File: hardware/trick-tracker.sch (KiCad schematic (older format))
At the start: 52 parts, among them J1 USB4105-GF-A, J2 S2B-PH-K, J3 QWiiC, J4 MEM2051-00-195-00-A, J5 Debug, J6 QWiiC, P1 SMTB-1240-S-R, U1 MS88SF2, U2 DPS368XTSA1, U3 LSM9DS1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

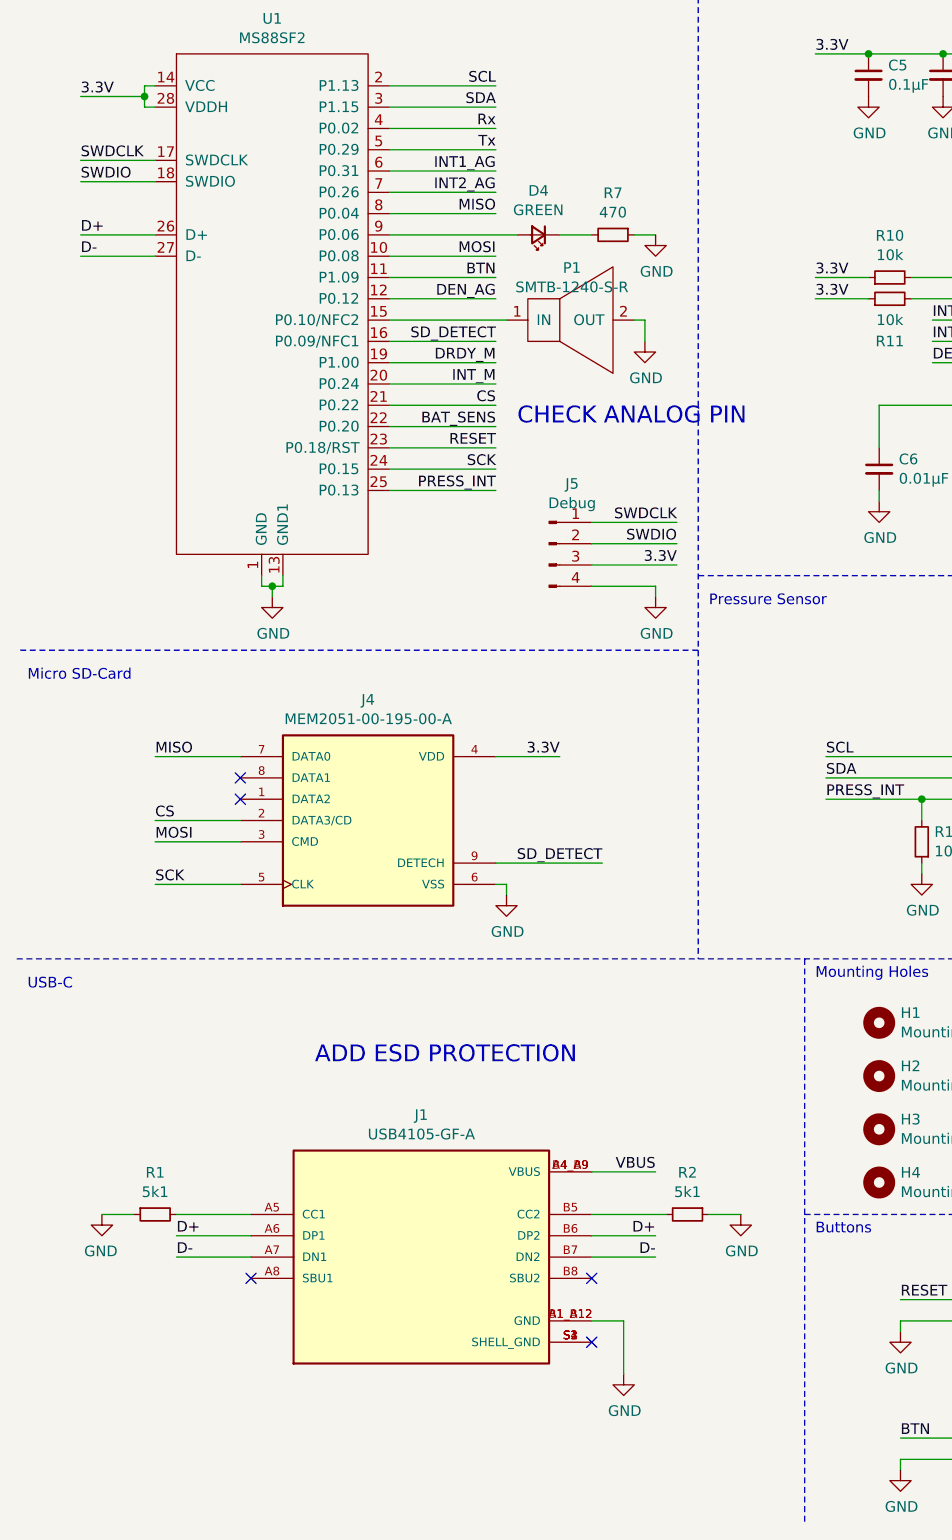
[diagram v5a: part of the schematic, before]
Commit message: Fix BAT_SENS and added it to an ADC - exchanged with an interrupt
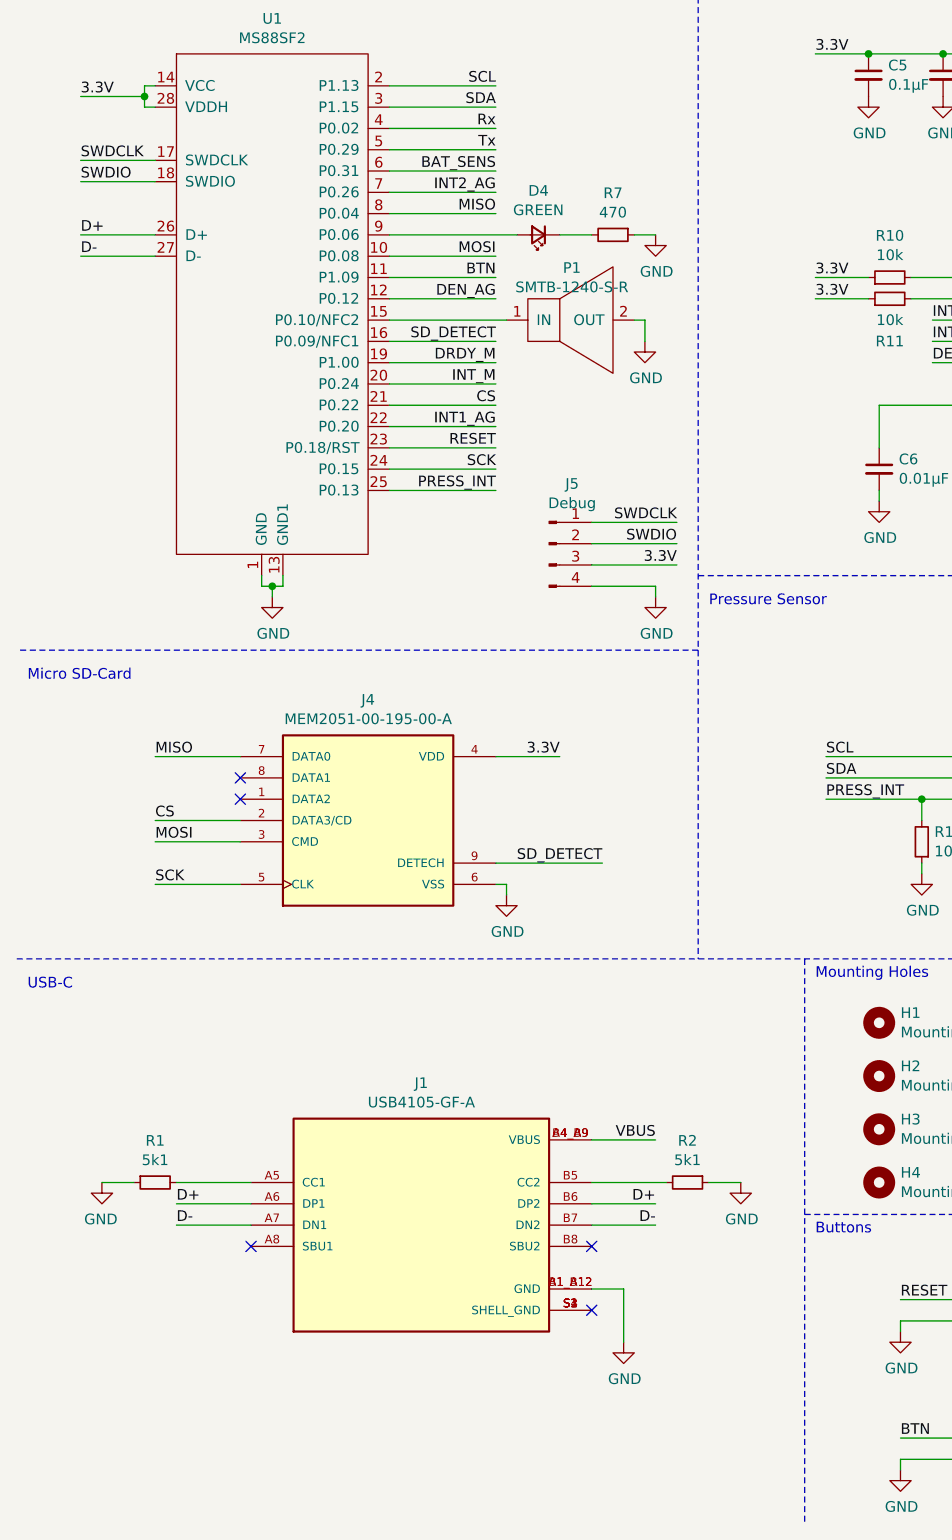
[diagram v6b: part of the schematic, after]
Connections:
- net BAT_SENS: now also U1.6 (P0.31); no longer U1.22 (P0.20)
- net INT1_AG: now also U1.22 (P0.20); no longer U1.6 (P0.31)
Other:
- note removed: "ADD ESD PROTECTION"
- note removed: "CHECK ANALOG PIN"
- moved on the sheet: J1, R1, R2
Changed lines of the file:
@@
 L USB4105-GF-A:USB4105-GF-A J1
 U 1 1 60A97D83
-P 2400 6550
-F 0 "J1" H 2400 7217 50  0000 C CNN
-F 1 "USB4105-GF-A" H 2400 7126 50  0000 C CNN
-F 2 "USB4105-GF-A:GCT_USB4105-GF-A" H 2400 6550 50  0001 L BNN
-F 3 "" H 2400 6550 50  0001 L BNN
-F 4 "A3" H 2400 6550 50  0001 L BNN "PARTREV"
-F 5 "3.31 mm" H 2400 6550 50  0001 L BNN "MAXIMUM_PACKAGE_HEIGHT"
-F 6 "Manufacturer Recommendations" H 2400 6550 50  0001 L BNN "STANDARD"
-F 7 "GCT" H 2400 6550 50  0001 L BNN "MANUFACTURER"
-	1    2400 6550
+P 2400 6400
+F 0 "J1" H 2400 7067 50  0000 C CNN
+F 1 "USB4105-GF-A" H 2400 6976 50  0000 C CNN
+F 2 "USB4105-GF-A:GCT_USB4105-GF-A" H 2400 6400 50  0001 L BNN
+F 3 "" H 2400 6400 50  0001 L BNN
+F 4 "A3" H 2400 6400 50  0001 L BNN "PARTREV"
+F 5 "3.31 mm" H 2400 6400 50  0001 L BNN "MAXIMUM_PACKAGE_HEIGHT"
+F 6 "Manufacturer Recommendations" H 2400 6400 50  0001 L BNN "STANDARD"
+F 7 "GCT" H 2400 6400 50  0001 L BNN "MANUFACTURER"
+	1    2400 6400
 	1    0    0    -1
 $EndComp
@@
 Wire Wire Line
 	10350 1700 10100 1700
-Text Label 3500 6150 2    50   ~ 0
+Text Label 3500 6000 2    50   ~ 0
 VBUS
-Text Label 3500 6450 2    50   ~ 0
+Text Label 3500 6300 2    50   ~ 0
 D+
-Text Label 3500 6550 2    50   ~ 0
+Text Label 3500 6400 2    50   ~ 0
 D-
-NoConn ~ 3200 6950
+NoConn ~ 3200 6800
 $Comp
 L power:GND #PWR0104
 U 1 1 60AA70B4
-P 3350 7100
-F 0 "#PWR0104" H 3350 6850 50  0001 C CNN
-F 1 "GND" H 3355 6927 50  0000 C CNN
-F 2 "" H 3350 7100 50  0001 C CNN
-F 3 "" H 3350 7100 50  0001 C CNN
-	1    3350 7100
-	1    0    0    -1
-$EndComp
-NoConn ~ 3200 6650
-NoConn ~ 1600 6650
-Text Label 1250 6450 0    50   ~ 0
+P 3350 6950
+F 0 "#PWR0104" H 3350 6700 50  0001 C CNN
+F 1 "GND" H 3355 6777 50  0000 C CNN
+F 2 "" H 3350 6950 50  0001 C CNN
+F 3 "" H 3350 6950 50  0001 C CNN
+	1    3350 6950
+	1    0    0    -1
+$EndComp
+NoConn ~ 3200 6500
+NoConn ~ 1600 6500
+Text Label 1250 6300 0    50   ~ 0
 D+
-Text Label 1250 6550 0    50   ~ 0
+Text Label 1250 6400 0    50   ~ 0
 D-
 Wire Wire Line
-	3500 6450 3200 6450
-Wire Wire Line
-	3500 6550 3200 6550
-Wire Wire Line
-	1600 6550 1250 6550
-Wire Wire Line
-	1250 6450 1600 6450
-Wire Wire Line
-	3500 6150 3200 6150
-Wire Wire Line
-	3200 6850 3350 6850
-Wire Wire Line
-	3350 6850 3350 7100
+	3500 6300 3200 6300
+Wire Wire Line
+	3500 6400 3200 6400
+Wire Wire Line
+	1600 6400 1250 6400
+Wire Wire Line
+	1250 6300 1600 6300
+Wire Wire Line
+	3500 6000 3200 6000
+Wire Wire Line
+	3200 6700 3350 6700
+Wire Wire Line
+	3350 6700 3350 6950
 Text Label 9750 2550 0    50   ~ 0
 VBUS
@@
 L Device:R_Small R1
 U 1 1 60AA9590
-P 1150 6350
-F 0 "R1" V 954 6350 50  0000 C CNN
-F 1 "5k1" V 1045 6350 50  0000 C CNN
-F 2 "Resistor_SMD:R_0603_1608Metric" H 1150 6350 50  0001 C CNN
-F 3 "~" H 1150 6350 50  0001 C CNN
-	1    1150 6350
+P 1150 6200
+F 0 "R1" V 954 6200 50  0000 C CNN
+F 1 "5k1" V 1045 6200 50  0000 C CNN
+F 2 "Resistor_SMD:R_0603_1608Metric" H 1150 6200 50  0001 C CNN
+F 3 "~" H 1150 6200 50  0001 C CNN
+	1    1150 6200
 	0    -1   1    0
 $EndComp
@@
 L Device:R_Small R2
 U 1 1 60AA9CB6
-P 3650 6350
-F 0 "R2" V 3454 6350 50  0000 C CNN
-F 1 "5k1" V 3545 6350 50  0000 C CNN
-F 2 "Resistor_SMD:R_0603_1608Metric" H 3650 6350 50  0001 C CNN
-F 3 "~" H 3650 6350 50  0001 C CNN
-	1    3650 6350
+P 3650 6200
+F 0 "R2" V 3454 6200 50  0000 C CNN
+F 1 "5k1" V 3545 6200 50  0000 C CNN
+F 2 "Resistor_SMD:R_0603_1608Metric" H 3650 6200 50  0001 C CNN
+F 3 "~" H 3650 6200 50  0001 C CNN
+	1    3650 6200
 	0    1    1    0
 $EndComp
 Wire Wire Line
-	1250 6350 1600 6350
-Wire Wire Line
-	3200 6350 3550 6350
+	1250 6200 1600 6200
+Wire Wire Line
+	3200 6200 3550 6200
 $Comp
 L power:GND #PWR0105
 U 1 1 60AAABDF
-P 3900 6350
-F 0 "#PWR0105" H 3900 6100 50  0001 C CNN
-F 1 "GND" H 3905 6177 50  0000 C CNN
-F 2 "" H 3900 6350 50  0001 C CNN
-F 3 "" H 3900 6350 50  0001 C CNN
-	1    3900 6350
+P 3900 6200
+F 0 "#PWR0105" H 3900 5950 50  0001 C CNN
+F 1 "GND" H 3905 6027 50  0000 C CNN
+F 2 "" H 3900 6200 50  0001 C CNN
+F 3 "" H 3900 6200 50  0001 C CNN
+	1    3900 6200
 	1    0    0    -1
 $EndComp
@@
 L power:GND #PWR0106
 U 1 1 60AAB5AF
-P 900 6350
-F 0 "#PWR0106" H 900 6100 50  0001 C CNN
-F 1 "GND" H 905 6177 50  0000 C CNN
-F 2 "" H 900 6350 50  0001 C CNN
-F 3 "" H 900 6350 50  0001 C CNN
-	1    900  6350
+P 900 6200
+F 0 "#PWR0106" H 900 5950 50  0001 C CNN
+F 1 "GND" H 905 6027 50  0000 C CNN
+F 2 "" H 900 6200 50  0001 C CNN
+F 3 "" H 900 6200 50  0001 C CNN
+	1    900  6200
 	-1   0    0    -1
 $EndComp
 Wire Wire Line
-	900  6350 1050 6350
-Wire Wire Line
-	3900 6350 3750 6350
+	900  6200 1050 6200
+Wire Wire Line
+	3900 6200 3750 6200
 Text Label 10900 2550 2    50   ~ 0
 STAT
@@
 Wire Wire Line
 	2750 1350 2250 1350
-Text Label 2750 1450 2    50   ~ 0
+Text Label 2750 2650 2    50   ~ 0
 INT1_AG
 Text Label 2750 1550 2    50   ~ 0
@@
 Wire Wire Line
 	9500 5800 10100 5800
-Text Label 2750 2650 2    50   ~ 0
+Text Label 2750 1450 2    50   ~ 0
 BAT_SENS
 Wire Wire Line
@@
 Wire Wire Line
 	3500 3400 3200 3400
-Text Notes 2850 2650 0    79   ~ 0
-CHECK ANALOG PIN
-Text Notes 1900 5650 0    79   ~ 0
-ADD ESD PROTECTION
 $Comp
 L SMTB-1240-S-R:SMTB-1240-S-R P1

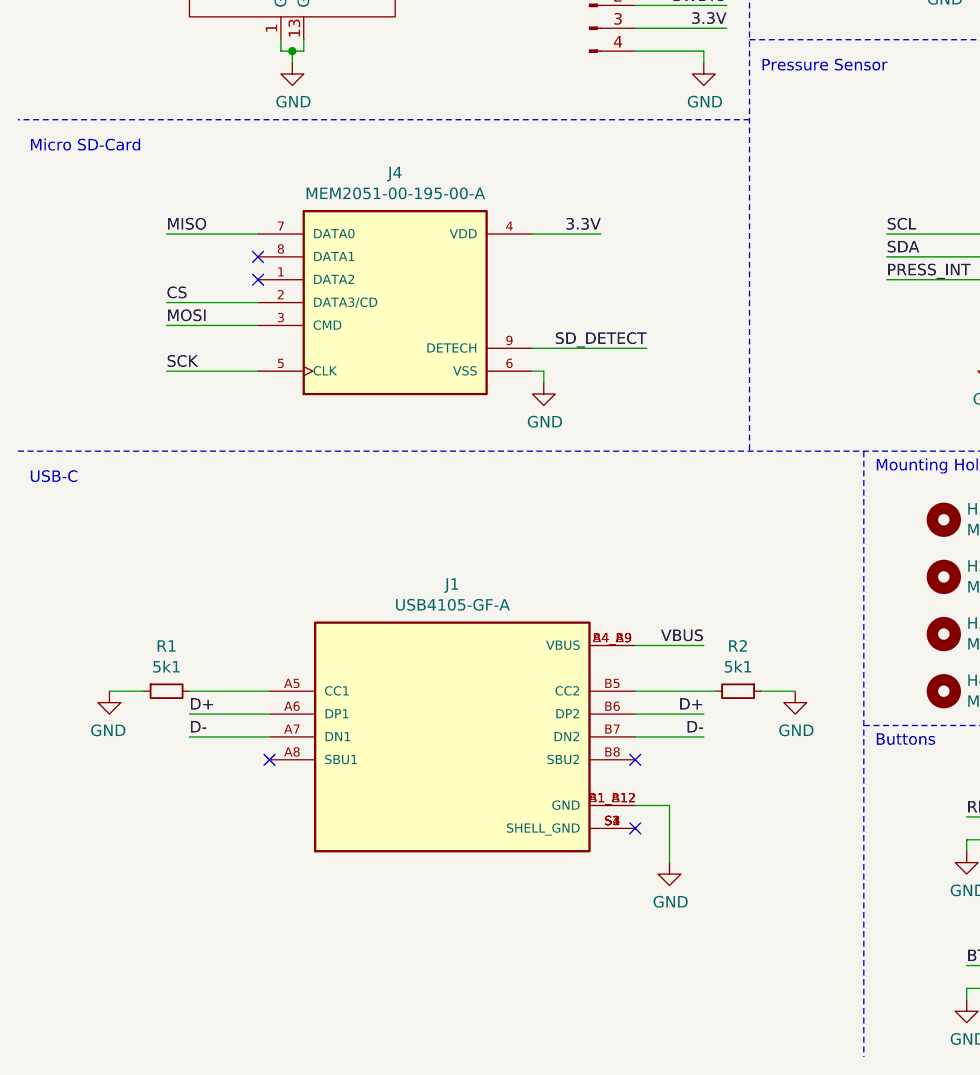
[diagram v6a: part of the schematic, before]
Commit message: Add ESD protection for USB
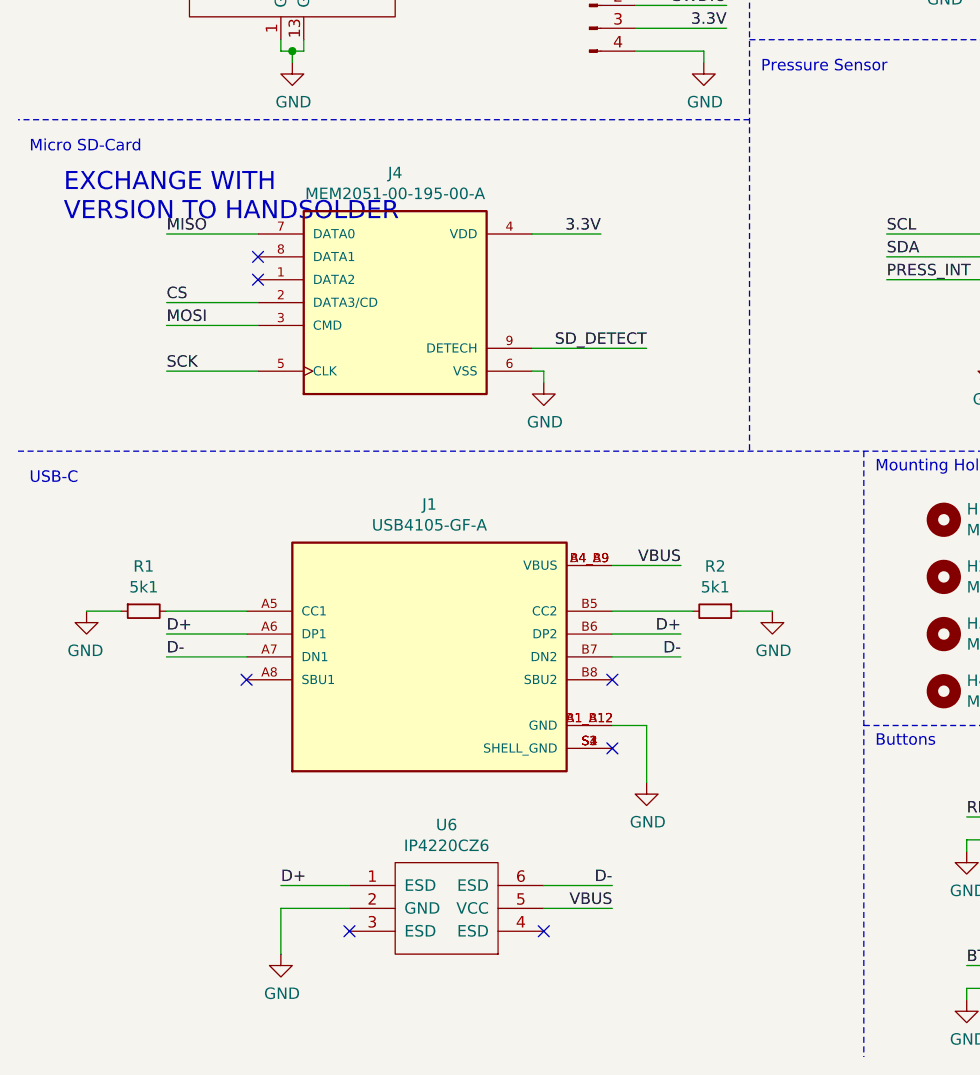
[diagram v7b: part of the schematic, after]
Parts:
- added U6: IP4220CZ6, Package_SO:TSOP-6_1.65x3.05mm_P0.95mm, symbol IP4220CZ6:IP4220CZ6
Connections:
- net D+: now also U6.1 (ESD)
- net D-: now also U6.6 (ESD)
- net GND: now also U6.2 (GND)
- net VBUS: now also U6.5 (VCC)
- no-connect marks 8 -> 10
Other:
- note added: "EXCHANGE WITH \nVERSION TO HANDSOLDER"
- moved on the sheet: J1, R1, R2
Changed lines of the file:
@@
 L USB4105-GF-A:USB4105-GF-A J1
 U 1 1 60A97D83
-P 2400 6400
-F 0 "J1" H 2400 7067 50  0000 C CNN
-F 1 "USB4105-GF-A" H 2400 6976 50  0000 C CNN
-F 2 "USB4105-GF-A:GCT_USB4105-GF-A" H 2400 6400 50  0001 L BNN
-F 3 "" H 2400 6400 50  0001 L BNN
-F 4 "A3" H 2400 6400 50  0001 L BNN "PARTREV"
-F 5 "3.31 mm" H 2400 6400 50  0001 L BNN "MAXIMUM_PACKAGE_HEIGHT"
-F 6 "Manufacturer Recommendations" H 2400 6400 50  0001 L BNN "STANDARD"
-F 7 "GCT" H 2400 6400 50  0001 L BNN "MANUFACTURER"
-	1    2400 6400
+P 2300 6050
+F 0 "J1" H 2300 6717 50  0000 C CNN
+F 1 "USB4105-GF-A" H 2300 6626 50  0000 C CNN
+F 2 "USB4105-GF-A:GCT_USB4105-GF-A" H 2300 6050 50  0001 L BNN
+F 3 "" H 2300 6050 50  0001 L BNN
+F 4 "A3" H 2300 6050 50  0001 L BNN "PARTREV"
+F 5 "3.31 mm" H 2300 6050 50  0001 L BNN "MAXIMUM_PACKAGE_HEIGHT"
+F 6 "Manufacturer Recommendations" H 2300 6050 50  0001 L BNN "STANDARD"
+F 7 "GCT" H 2300 6050 50  0001 L BNN "MANUFACTURER"
+	1    2300 6050
 	1    0    0    -1
 $EndComp
@@
 Wire Wire Line
 	10350 1700 10100 1700
-Text Label 3500 6000 2    50   ~ 0
+Text Label 3400 5650 2    50   ~ 0
 VBUS
-Text Label 3500 6300 2    50   ~ 0
+Text Label 3400 5950 2    50   ~ 0
 D+
-Text Label 3500 6400 2    50   ~ 0
+Text Label 3400 6050 2    50   ~ 0
 D-
-NoConn ~ 3200 6800
+NoConn ~ 3100 6450
 $Comp
 L power:GND #PWR0104
 U 1 1 60AA70B4
-P 3350 6950
-F 0 "#PWR0104" H 3350 6700 50  0001 C CNN
-F 1 "GND" H 3355 6777 50  0000 C CNN
-F 2 "" H 3350 6950 50  0001 C CNN
-F 3 "" H 3350 6950 50  0001 C CNN
-	1    3350 6950
-	1    0    0    -1
-$EndComp
-NoConn ~ 3200 6500
-NoConn ~ 1600 6500
-Text Label 1250 6300 0    50   ~ 0
+P 3250 6600
+F 0 "#PWR0104" H 3250 6350 50  0001 C CNN
+F 1 "GND" H 3255 6427 50  0000 C CNN
+F 2 "" H 3250 6600 50  0001 C CNN
+F 3 "" H 3250 6600 50  0001 C CNN
+	1    3250 6600
+	1    0    0    -1
+$EndComp
+NoConn ~ 3100 6150
+NoConn ~ 1500 6150
+Text Label 1150 5950 0    50   ~ 0
 D+
-Text Label 1250 6400 0    50   ~ 0
+Text Label 1150 6050 0    50   ~ 0
 D-
 Wire Wire Line
-	3500 6300 3200 6300
-Wire Wire Line
-	3500 6400 3200 6400
-Wire Wire Line
-	1600 6400 1250 6400
-Wire Wire Line
-	1250 6300 1600 6300
-Wire Wire Line
-	3500 6000 3200 6000
-Wire Wire Line
-	3200 6700 3350 6700
-Wire Wire Line
-	3350 6700 3350 6950
+	3400 5950 3100 5950
+Wire Wire Line
+	3400 6050 3100 6050
+Wire Wire Line
+	1500 6050 1150 6050
+Wire Wire Line
+	1150 5950 1500 5950
+Wire Wire Line
+	3400 5650 3100 5650
+Wire Wire Line
+	3100 6350 3250 6350
+Wire Wire Line
+	3250 6350 3250 6600
 Text Label 9750 2550 0    50   ~ 0
 VBUS
@@
 L Device:R_Small R1
 U 1 1 60AA9590
-P 1150 6200
-F 0 "R1" V 954 6200 50  0000 C CNN
-F 1 "5k1" V 1045 6200 50  0000 C CNN
-F 2 "Resistor_SMD:R_0603_1608Metric" H 1150 6200 50  0001 C CNN
-F 3 "~" H 1150 6200 50  0001 C CNN
-	1    1150 6200
+P 1050 5850
+F 0 "R1" V 854 5850 50  0000 C CNN
+F 1 "5k1" V 945 5850 50  0000 C CNN
+F 2 "Resistor_SMD:R_0603_1608Metric" H 1050 5850 50  0001 C CNN
+F 3 "~" H 1050 5850 50  0001 C CNN
+	1    1050 5850
 	0    -1   1    0
 $EndComp
@@
 L Device:R_Small R2
 U 1 1 60AA9CB6
-P 3650 6200
-F 0 "R2" V 3454 6200 50  0000 C CNN
-F 1 "5k1" V 3545 6200 50  0000 C CNN
-F 2 "Resistor_SMD:R_0603_1608Metric" H 3650 6200 50  0001 C CNN
-F 3 "~" H 3650 6200 50  0001 C CNN
-	1    3650 6200
+P 3550 5850
+F 0 "R2" V 3354 5850 50  0000 C CNN
+F 1 "5k1" V 3445 5850 50  0000 C CNN
+F 2 "Resistor_SMD:R_0603_1608Metric" H 3550 5850 50  0001 C CNN
+F 3 "~" H 3550 5850 50  0001 C CNN
+	1    3550 5850
 	0    1    1    0
 $EndComp
 Wire Wire Line
-	1250 6200 1600 6200
-Wire Wire Line
-	3200 6200 3550 6200
+	1150 5850 1500 5850
+Wire Wire Line
+	3100 5850 3450 5850
 $Comp
 L power:GND #PWR0105
 U 1 1 60AAABDF
-P 3900 6200
-F 0 "#PWR0105" H 3900 5950 50  0001 C CNN
-F 1 "GND" H 3905 6027 50  0000 C CNN
-F 2 "" H 3900 6200 50  0001 C CNN
-F 3 "" H 3900 6200 50  0001 C CNN
-	1    3900 6200
+P 3800 5850
+F 0 "#PWR0105" H 3800 5600 50  0001 C CNN
+F 1 "GND" H 3805 5677 50  0000 C CNN
+F 2 "" H 3800 5850 50  0001 C CNN
+F 3 "" H 3800 5850 50  0001 C CNN
+	1    3800 5850
 	1    0    0    -1
 $EndComp
@@
 L power:GND #PWR0106
 U 1 1 60AAB5AF
-P 900 6200
-F 0 "#PWR0106" H 900 5950 50  0001 C CNN
-F 1 "GND" H 905 6027 50  0000 C CNN
-F 2 "" H 900 6200 50  0001 C CNN
-F 3 "" H 900 6200 50  0001 C CNN
-	1    900  6200
+P 800 5850
+F 0 "#PWR0106" H 800 5600 50  0001 C CNN
+F 1 "GND" H 805 5677 50  0000 C CNN
+F 2 "" H 800 5850 50  0001 C CNN
+F 3 "" H 800 5850 50  0001 C CNN
+	1    800  5850
 	-1   0    0    -1
 $EndComp
 Wire Wire Line
-	900  6200 1050 6200
-Wire Wire Line
-	3900 6200 3750 6200
+	800  5850 950  5850
+Wire Wire Line
+	3800 5850 3650 5850
 Text Label 10900 2550 2    50   ~ 0
 STAT
@@
 Wire Wire Line
 	7600 5700 7900 5700
+$Comp
+L IP4220CZ6:IP4220CZ6 U6
+U 1 1 60B113A2
+P 2450 7100
+F 0 "U6" H 2375 7415 50  0000 C CNN
+F 1 "IP4220CZ6" H 2375 7324 50  0000 C CNN
+F 2 "Package_SO:TSOP-6_1.65x3.05mm_P0.95mm" H 2450 7100 50  0001 C CNN
+F 3 "" H 2450 7100 50  0001 C CNN
+	1    2450 7100
+	1    0    0    -1
+$EndComp
+Text Label 1650 7050 0    50   ~ 0
+D+
+Text Label 3100 7050 2    50   ~ 0
+D-
+Text Label 3100 7150 2    50   ~ 0
+VBUS
+$Comp
+L power:GND #PWR0135
+U 1 1 60B11942
+P 1650 7350
+F 0 "#PWR0135" H 1650 7100 50  0001 C CNN
+F 1 "GND" H 1655 7177 50  0000 C CNN
+F 2 "" H 1650 7350 50  0001 C CNN
+F 3 "" H 1650 7350 50  0001 C CNN
+	1    1650 7350
+	1    0    0    -1
+$EndComp
+Wire Wire Line
+	1950 7050 1650 7050
+Wire Wire Line
+	2800 7050 3100 7050
+Wire Wire Line
+	3100 7150 2800 7150
+Wire Wire Line
+	1950 7150 1650 7150
+Wire Wire Line
+	1650 7150 1650 7350
+NoConn ~ 2800 7250
+NoConn ~ 1950 7250
+Text Notes 700  4150 0    79   ~ 0
+EXCHANGE WITH \nVERSION TO HANDSOLDER
 $EndSCHEMATC
